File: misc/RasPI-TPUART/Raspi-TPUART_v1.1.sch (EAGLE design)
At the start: 27 parts, among them Q1 4,915MHz

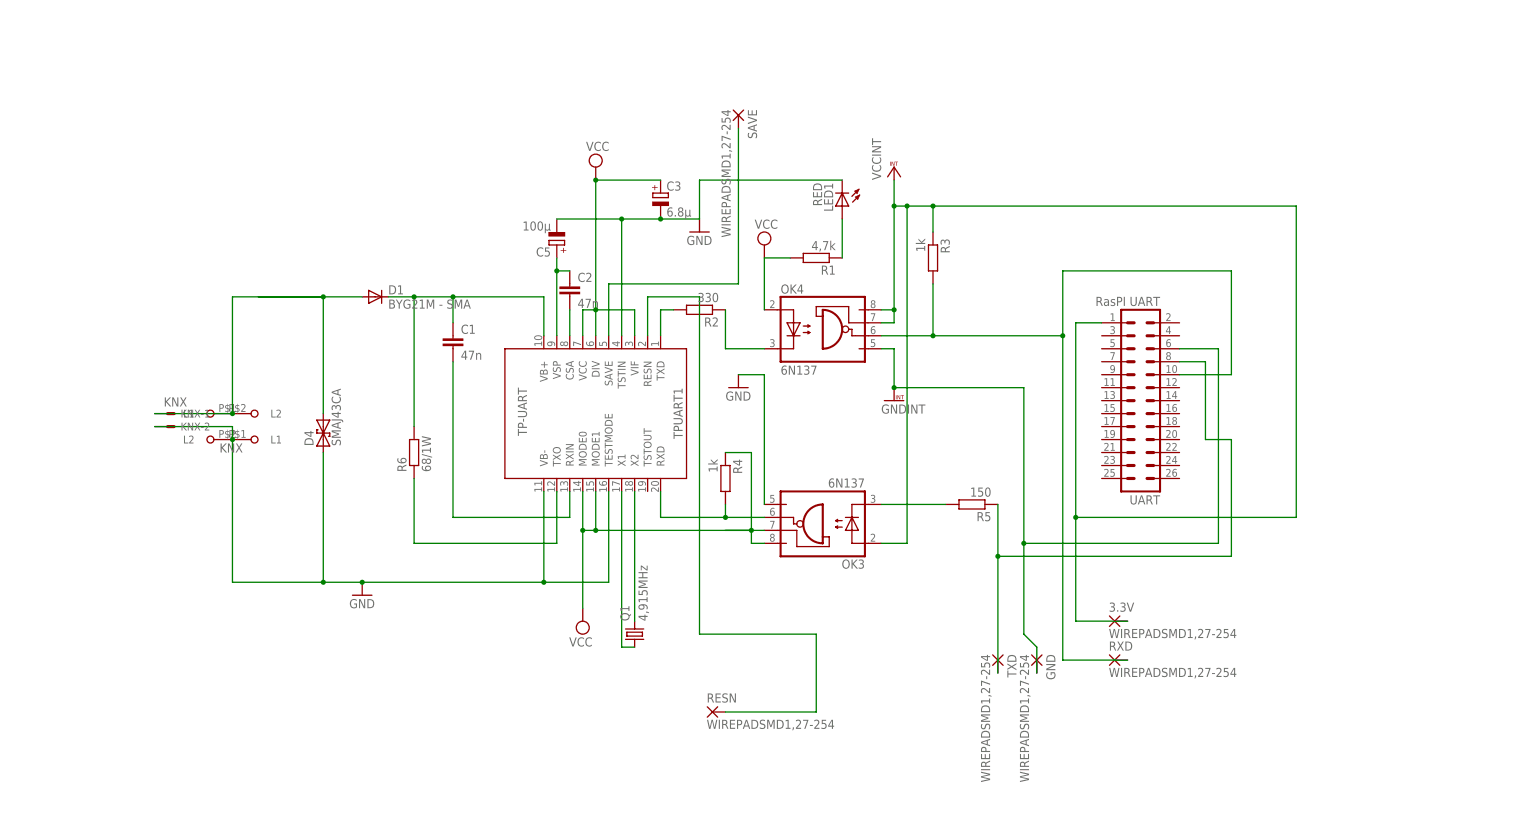
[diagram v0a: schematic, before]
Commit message: Add rx and tx led. Optional. Bridge the led pads, if no need.
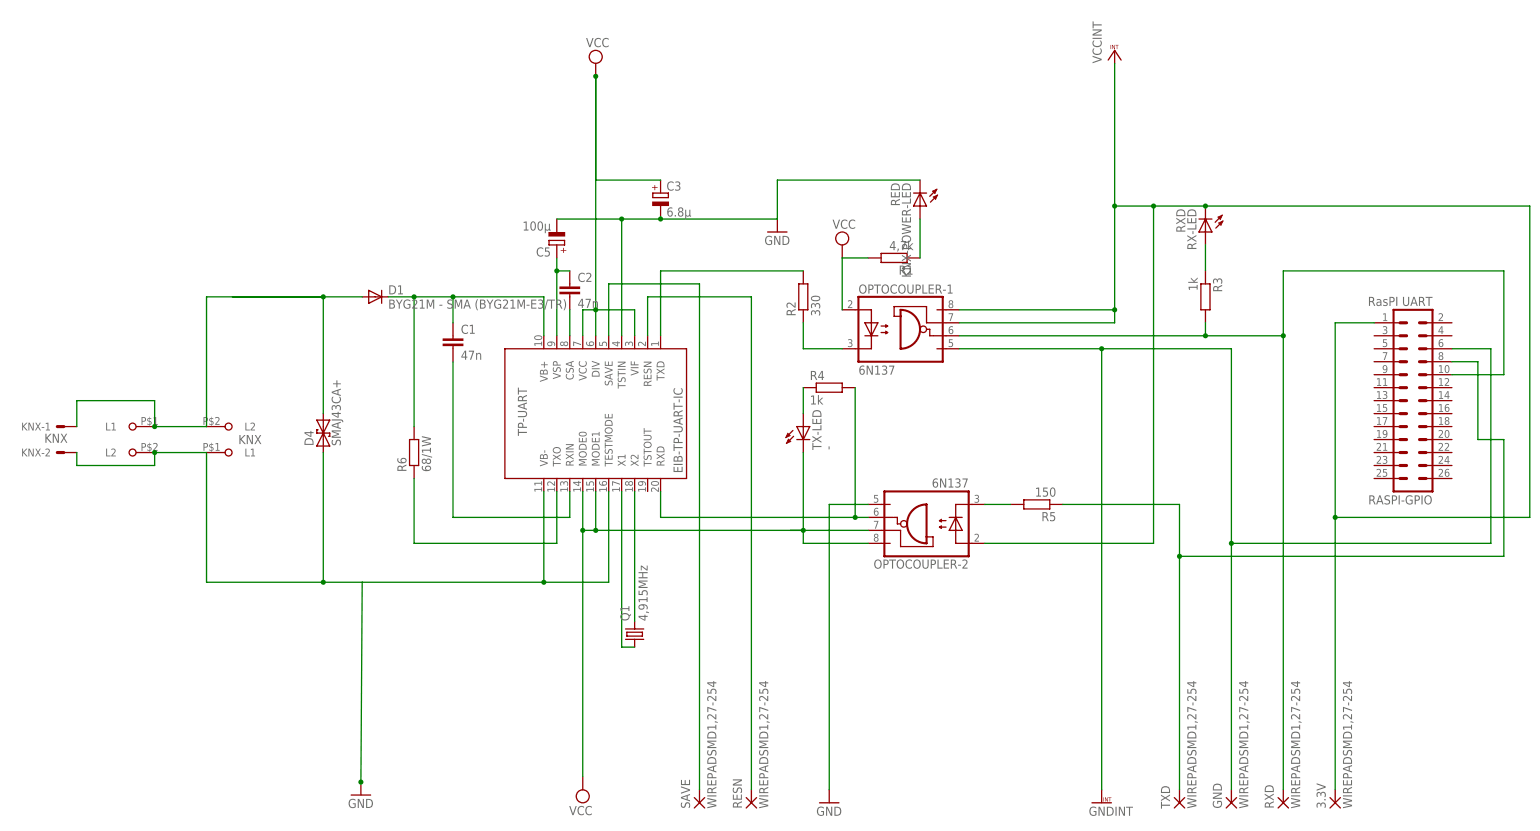
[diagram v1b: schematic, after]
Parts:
- removed LED1: RED, led:LEDKA-3528ASYC
- removed OK3, OK4: 6N137, optocoupler:6N137
- removed UART: RasPI UART, con-lstb:MA13-2
- added KNX-POWER-LED: RED, led:LEDKA-3528ASYC
- added OPTOCOUPLER-1, OPTOCOUPLER-2: 6N137, optocoupler:6N137
- added RASPI-GPIO: RasPI UART, con-lstb:MA13-2
- added RX-LED: RXD, led:LEDKA-3528ASYC
- added TX-LED: -, led:LEDKA-3528ASYC
- D1: value BYG21M - SMA -> BYG21M - SMA (BYG21M-E3/TR)
- D4: value SMAJ43CA -> SMAJ43CA+
- renumbered TPUART1 to EIB-TP-UART-IC
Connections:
- new net N$1: R3.1, RX-LED.A
- new net N$3: R4.1, TX-LED.A
- net GND: now also KNX-POWER-LED.C, OPTOCOUPLER-2.GND; no longer LED1.C, OK3.GND
- net GNDINT: now also OPTOCOUPLER-1.GND, RASPI-GPIO.6; no longer OK4.GND, UART.6
- net N$14: now also OPTOCOUPLER-2.C; no longer OK3.C
- net N$18: now also KNX-POWER-LED.A; no longer LED1.A
- net RASPI_RXD: now also OPTOCOUPLER-1.VO, RASPI-GPIO.10; no longer OK4.VO, UART.10
- net RASPI_TXD: now also RASPI-GPIO.8; no longer UART.8
- net RXD: now also OPTOCOUPLER-2.VO; no longer OK3.VO
- net TXD1: now also OPTOCOUPLER-1.C; no longer OK4.C
- net VCC: now also OPTOCOUPLER-1.A, OPTOCOUPLER-2.VCC, OPTOCOUPLER-2.VE, TX-LED.C; no longer OK3.VCC, OK3.VE, OK4.A, R4.1
- net VCCINT: now also OPTOCOUPLER-1.VCC, OPTOCOUPLER-1.VE, OPTOCOUPLER-2.A, RASPI-GPIO.1, RX-LED.C; no longer OK3.A, OK4.VCC, OK4.VE, R3.1, UART.1
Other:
- moved on the sheet: 3.3V, GND, KNX-1, KNX-2, R1, R2, R3, R4, R5, RESN, RXD, SAVE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
